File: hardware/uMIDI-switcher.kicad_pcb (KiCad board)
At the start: 2 copper layers, 127 x 50 mm, 107 parts, among them Q1 BSS138, Q2 BSS138, Q3 BSS138, Q4 BSS138, Q5 BSS138, Q6 BSS138, Q7 BSS138, Q8 BSS138, U1 MC7809CD, U2 MC7809CD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

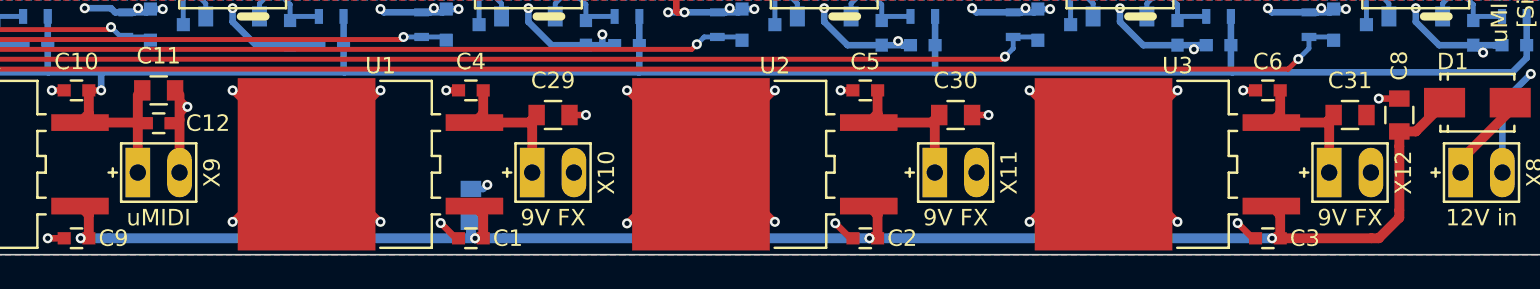
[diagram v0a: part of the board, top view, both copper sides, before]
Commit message: Increase size of polarity markers
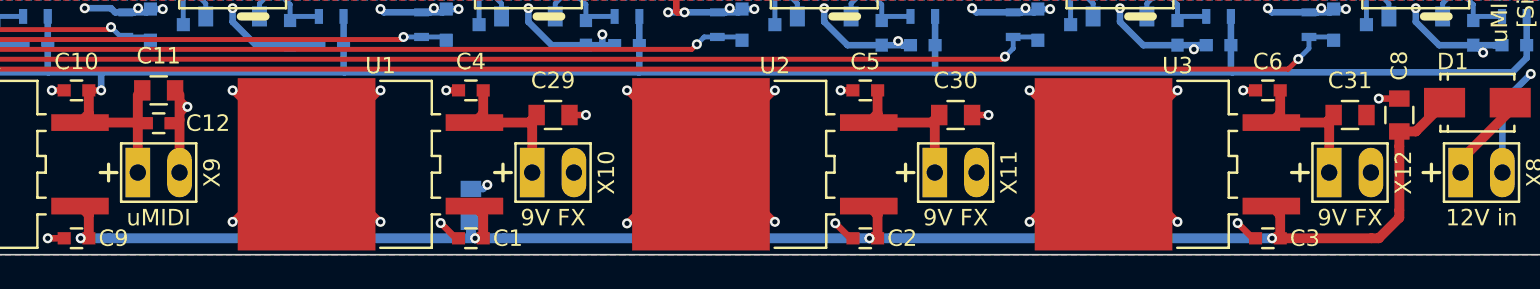
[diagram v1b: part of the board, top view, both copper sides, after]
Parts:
- X10: footprint uMIDI-switcher:PINHEAD-Supply -> PINHEAD-Supply
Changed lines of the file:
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@@
     (links 269)
     (no_connects 0)
-    (area 77.449999 78.949999 204.550001 129.050001)
+    (area 77.449999 69.824999 205.025 129.275001)
     (thickness 1.6)
     (drawings 12)
@@
   (page A4)
   (layers
-    (0 F.Cu signal hide)
+    (0 F.Cu signal)
     (31 B.Cu signal)
     (32 B.Adhes user)
@@
     (add_net GND)
   )
+  (module PINHEAD-Supply (layer F.Cu)
+    (at 144 124)
+    (attr virtual)
+    (fp_text reference X10 (at 3.25 0 90) (layer F.SilkS)
+      (effects (font (size 1 1) (thickness 0.15)))
+    )
+    (fp_text value CONN_01X02 (at 0 3.81) (layer F.Fab)
+      (effects (font (size 1 1) (thickness 0.15)))
+    )
+    (fp_line (start -3.556 0) (end -2.54 0) (layer F.SilkS) (width 0.2))
+    (fp_line (start -3.048 -0.508) (end -3.048 0.508) (layer F.SilkS) (width 0.2))
+    (fp_line (start 2.286 1.778) (end -2.286 1.778) (layer F.SilkS) (width 0.15))
+    (fp_line (start -2.286 -1.778) (end 2.286 -1.778) (layer F.SilkS) (width 0.15))
+    (fp_line (start -2.286 -1.778) (end -2.286 1.778) (layer F.SilkS) (width 0.15))
+    (fp_line (start 2.286 -1.778) (end 2.286 1.778) (layer F.SilkS) (width 0.15))
+    (pad 1 thru_hole rect (at -1.27 0) (size 1.50622 3.01498) (drill 0.99822) (layers *.Cu *.Mask)
+      (net 57 "Net-(C29-Pad1)"))
+    (pad 2 thru_hole oval (at 1.27 0) (size 1.50622 3.01498) (drill 0.99822) (layers *.Cu *.Mask)
+      (net 1 GND) (zone_connect 2))
+  )
   (module uMIDI-switcher:Omron_G6K-2P (layer F.Cu)
     (at 178.5 109 90)
@@
   )
   (module uMIDI-switcher:PINHEAD-Supply (layer F.Cu)
-    (at 192.5 124)
+    (at 200.5 124)
     (attr virtual)
-    (fp_text reference X12 (at 3.25 0 90) (layer F.SilkS)
+    (fp_text reference X8 (at 3.25 0 90) (layer F.SilkS)
       (effects (font (size 1 1) (thickness 0.15)))
     )
-    (fp_text value CONN_01X02 (at 0 3.81) (layer F.Fab)
+    (fp_text value "12V in" (at 0 3.81) (layer F.Fab)
       (effects (font (size 1 1) (thickness 0.15)))
     )
-    (fp_line (start -3.048 0) (end -2.54 0) (layer F.SilkS) (width 0.15))
-    (fp_line (start -2.794 -0.254) (end -2.794 0.254) (layer F.SilkS) (width 0.15))
+    (fp_line (start -3.556 0) (end -2.54 0) (layer F.SilkS) (width 0.2))
+    (fp_line (start -3.048 -0.508) (end -3.048 0.508) (layer F.SilkS) (width 0.2))
     (fp_line (start 2.286 1.778) (end -2.286 1.778) (layer F.SilkS) (width 0.15))
     (fp_line (start -2.286 -1.778) (end 2.286 -1.778) (layer F.SilkS) (width 0.15))
@@
     (fp_line (start 2.286 -1.778) (end 2.286 1.778) (layer F.SilkS) (width 0.15))
     (pad 1 thru_hole rect (at -1.27 0) (size 1.50622 3.01498) (drill 0.99822) (layers *.Cu *.Mask)
-      (net 59 "Net-(C31-Pad1)"))
+      (net 5 /pwr_in))
     (pad 2 thru_hole oval (at 1.27 0) (size 1.50622 3.01498) (drill 0.99822) (layers *.Cu *.Mask)
       (net 1 GND) (zone_connect 2))
   )
   (module uMIDI-switcher:PINHEAD-Supply (layer F.Cu)
-    (at 168.5 124)
+    (at 120 124)
     (attr virtual)
-    (fp_text reference X11 (at 3.25 0 90) (layer F.SilkS)
+    (fp_text reference X9 (at 3.25 0 90) (layer F.SilkS)
       (effects (font (size 1 1) (thickness 0.15)))
     )
-    (fp_text value CONN_01X02 (at 0 3.81) (layer F.Fab)
+    (fp_text value "uMIDI Power" (at 0 3.81) (layer F.Fab)
       (effects (font (size 1 1) (thickness 0.15)))
     )
-    (fp_line (start -3.048 0) (end -2.54 0) (layer F.SilkS) (width 0.15))
-    (fp_line (start -2.794 -0.254) (end -2.794 0.254) (layer F.SilkS) (width 0.15))
+    (fp_line (start -3.556 0) (end -2.54 0) (layer F.SilkS) (width 0.2))
+    (fp_line (start -3.048 -0.508) (end -3.048 0.508) (layer F.SilkS) (width 0.2))
     (fp_line (start 2.286 1.778) (end -2.286 1.778) (layer F.SilkS) (width 0.15))
     (fp_line (start -2.286 -1.778) (end 2.286 -1.778) (layer F.SilkS) (width 0.15))
@@
     (fp_line (start 2.286 -1.778) (end 2.286 1.778) (layer F.SilkS) (width 0.15))
     (pad 1 thru_hole rect (at -1.27 0) (size 1.50622 3.01498) (drill 0.99822) (layers *.Cu *.Mask)
-      (net 58 "Net-(C30-Pad1)"))
+      (net 3 +9V))
     (pad 2 thru_hole oval (at 1.27 0) (size 1.50622 3.01498) (drill 0.99822) (layers *.Cu *.Mask)
       (net 1 GND) (zone_connect 2))
   )
   (module uMIDI-switcher:PINHEAD-Supply (layer F.Cu)
-    (at 144 124)
+    (at 168.5 124)
     (attr virtual)
-    (fp_text reference X10 (at 3.25 0 90) (layer F.SilkS)
+    (fp_text reference X11 (at 3.25 0 90) (layer F.SilkS)
       (effects (font (size 1 1) (thickness 0.15)))
     )
@@
       (effects (font (size 1 1) (thickness 0.15)))
     )
-    (fp_line (start -3.048 0) (end -2.54 0) (layer F.SilkS) (width 0.15))
-    (fp_line (start -2.794 -0.254) (end -2.794 0.254) (layer F.SilkS) (width 0.15))
-    (fp_line (start 2.286 1.778) (end -2.286 1.778) (layer F.SilkS) (width 0.15))
-    (fp_line (start -2.286 -1.778) (end 2.286 -1.778) (layer F.SilkS) (width 0.15))
-    (fp_line (start -2.286 -1.778) (end -2.286 1.778) (layer F.SilkS) (width 0.15))
-    (fp_line (start 2.286 -1.778) (end 2.286 1.778) (layer F.SilkS) (width 0.15))
-    (pad 1 thru_hole rect (at -1.27 0) (size 1.50622 3.01498) (drill 0.99822) (layers *.Cu *.Mask)
-      (net 57 "Net-(C29-Pad1)"))
-    (pad 2 thru_hole oval (at 1.27 0) (size 1.50622 3.01498) (drill 0.99822) (layers *.Cu *.Mask)
-      (net 1 GND) (zone_connect 2))
-  )
-  (module uMIDI-switcher:PINHEAD-Supply (layer F.Cu)
-    (at 120 124)
-    (attr virtual)
-    (fp_text reference X9 (at 3.25 0 90) (layer F.SilkS)
-      (effects (font (size 1 1) (thickness 0.15)))
-    )
-    (fp_text value "uMIDI Power" (at 0 3.81) (layer F.Fab)
-      (effects (font (size 1 1) (thickness 0.15)))
-    )
-    (fp_line (start -3.048 0) (end -2.54 0) (layer F.SilkS) (width 0.15))
-    (fp_line (start -2.794 -0.254) (end -2.794 0.254) (layer F.SilkS) (width 0.15))
+    (fp_line (start -3.556 0) (end -2.54 0) (layer F.SilkS) (width 0.2))
+    (fp_line (start -3.048 -0.508) (end -3.048 0.508) (layer F.SilkS) (width 0.2))
     (fp_line (start 2.286 1.778) (end -2.286 1.778) (layer F.SilkS) (width 0.15))
     (fp_line (start -2.286 -1.778) (end 2.286 -1.778) (layer F.SilkS) (width 0.15))
@@
     (fp_line (start 2.286 -1.778) (end 2.286 1.778) (layer F.SilkS) (width 0.15))
     (pad 1 thru_hole rect (at -1.27 0) (size 1.50622 3.01498) (drill 0.99822) (layers *.Cu *.Mask)
-      (net 3 +9V))
+      (net 58 "Net-(C30-Pad1)"))
     (pad 2 thru_hole oval (at 1.27 0) (size 1.50622 3.01498) (drill 0.99822) (layers *.Cu *.Mask)
       (net 1 GND) (zone_connect 2))
   )
   (module uMIDI-switcher:PINHEAD-Supply (layer F.Cu)
-    (at 200.5 124)
+    (at 192.5 124)
     (attr virtual)
-    (fp_text reference X8 (at 3.25 0 90) (layer F.SilkS)
+    (fp_text reference X12 (at 3.25 0 90) (layer F.SilkS)
       (effects (font (size 1 1) (thickness 0.15)))
     )
-    (fp_text value "12V in" (at 0 3.81) (layer F.Fab)
+    (fp_text value CONN_01X02 (at 0 3.81) (layer F.Fab)
       (effects (font (size 1 1) (thickness 0.15)))
     )
-    (fp_line (start -3.048 0) (end -2.54 0) (layer F.SilkS) (width 0.15))
-    (fp_line (start -2.794 -0.254) (end -2.794 0.254) (layer F.SilkS) (width 0.15))
+    (fp_line (start -3.556 0) (end -2.54 0) (layer F.SilkS) (width 0.2))
+    (fp_line (start -3.048 -0.508) (end -3.048 0.508) (layer F.SilkS) (width 0.2))
     (fp_line (start 2.286 1.778) (end -2.286 1.778) (layer F.SilkS) (width 0.15))
     (fp_line (start -2.286 -1.778) (end 2.286 -1.778) (layer F.SilkS) (width 0.15))
@@
     (fp_line (start 2.286 -1.778) (end 2.286 1.778) (layer F.SilkS) (width 0.15))
     (pad 1 thru_hole rect (at -1.27 0) (size 1.50622 3.01498) (drill 0.99822) (layers *.Cu *.Mask)
-      (net 5 /pwr_in))
+      (net 59 "Net-(C31-Pad1)"))
     (pad 2 thru_hole oval (at 1.27 0) (size 1.50622 3.01498) (drill 0.99822) (layers *.Cu *.Mask)
       (net 1 GND) (zone_connect 2))

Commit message: Add backside drill plan
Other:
- board text added: "14x 11mm hole"
- board text added: "Case bottom"
- board text added: "PCB"
- board text added: "Proposed housing: Hammond 1550Z116(BK)"

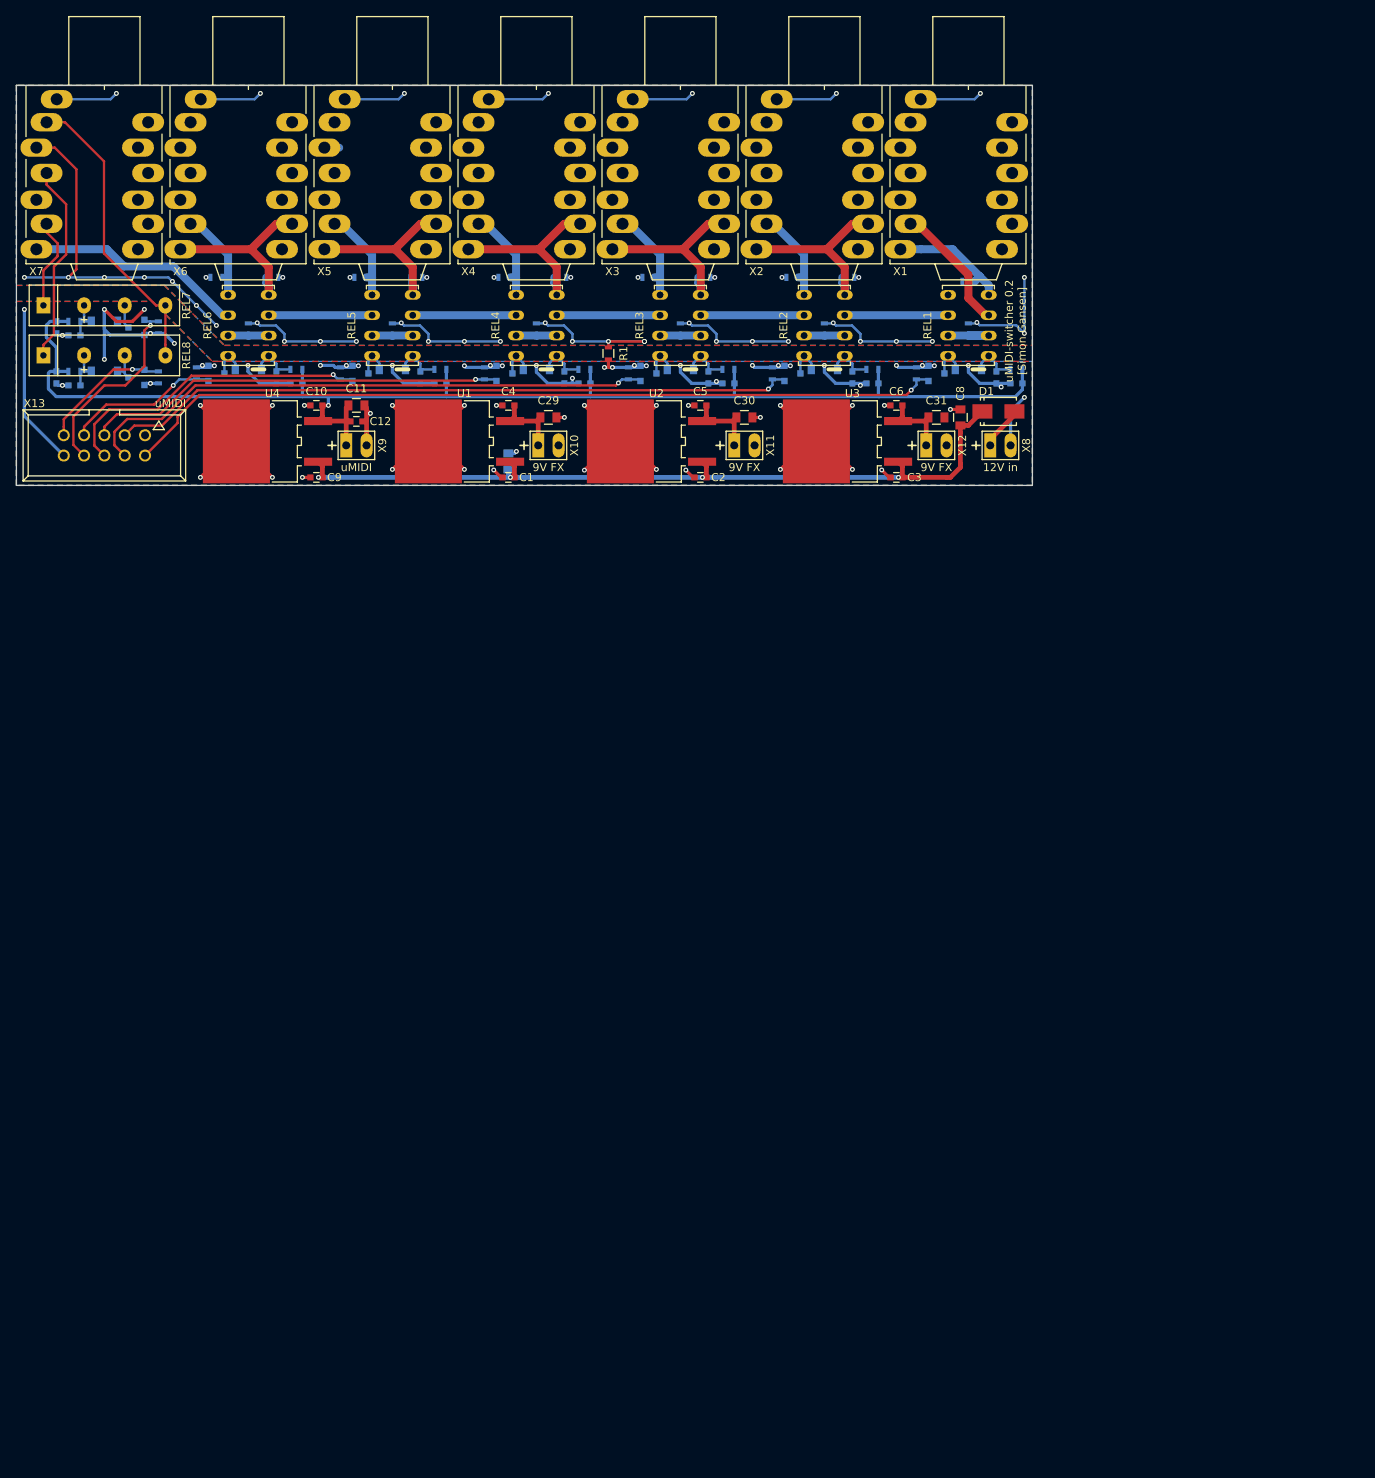
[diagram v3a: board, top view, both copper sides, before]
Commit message: Add control panel concept and drawing
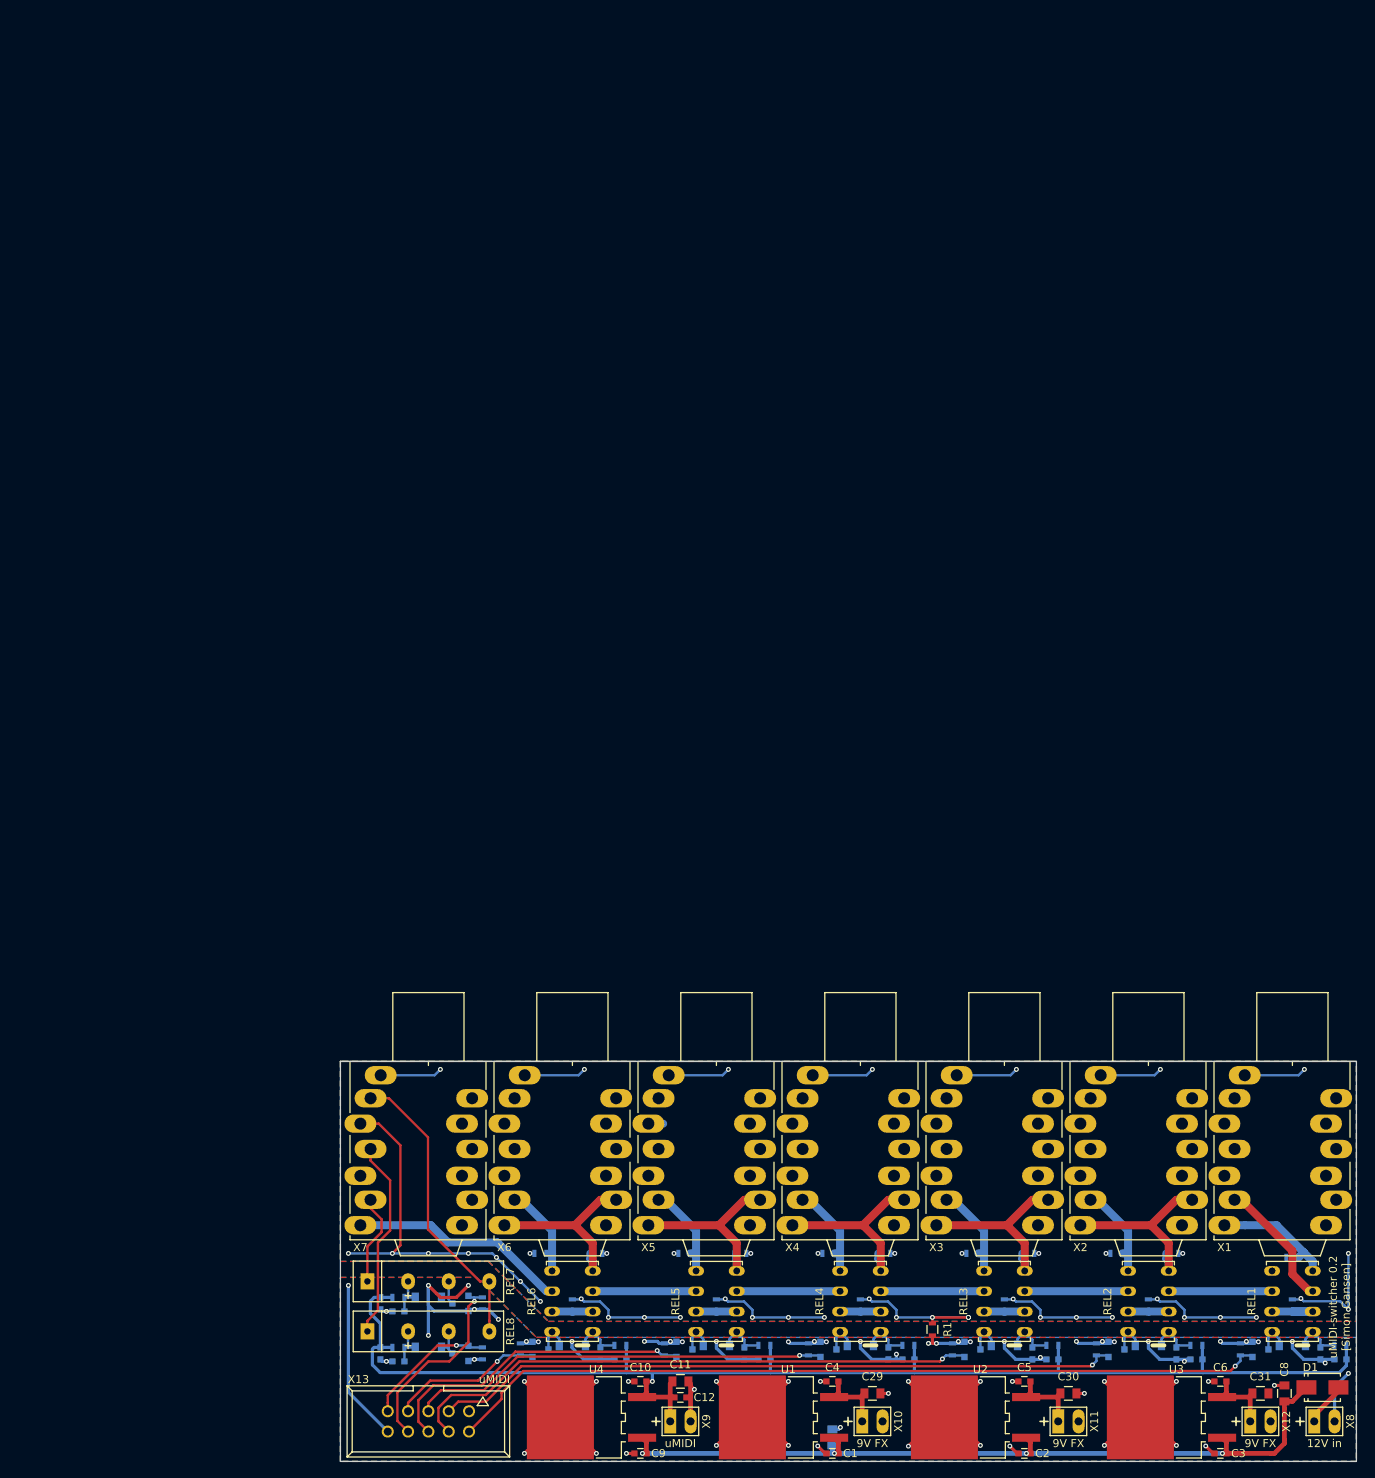
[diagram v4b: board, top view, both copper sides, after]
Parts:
- moved C1 128.5 mm to (179.5, 250.0)
- moved C10 128.5 mm to (155.5, 241.0)
- moved C11 128.5 mm to (160.5, 241.0)
- moved C12 128.5 mm to (160.5, 243.0)
- moved C13 128.5 mm to (243.0, 238.2)
- moved C14 128.5 mm to (240.5, 237.5)
- moved C15 128.5 mm to (207.0, 238.2)
- moved C16 128.5 mm to (204.5, 237.5)
- moved C17 128.5 mm to (189.0, 238.2)
- moved C18 128.5 mm to (186.5, 237.5)
- moved C19 128.5 mm to (171.0, 238.2)
- moved C2 128.5 mm to (203.5, 250.0)
- moved C20 128.5 mm to (168.5, 237.5)
- moved C21 128.5 mm to (153.0, 238.2)
- moved C22 128.5 mm to (150.5, 237.5)
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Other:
- board text added: "Loop1"
- board text added: "Loop2"
- board text added: "Loop3"
- board text added: "Loop4"
- board text added: "Loop5"
- board text added: "Mute/Tune"
- board text added: "SW Ring"
- board text added: "SW Tip"
- board text added: "Save"

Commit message: Revise control panel drawing
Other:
- board text added: "14x 11mm holes"
- board text added: "Lid"
- board text added: "Rear"
- board text removed: "14x 11mm hole"
